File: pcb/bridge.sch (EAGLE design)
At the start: 38 parts, among them IC2 LM358D, IC3 78L05SMD, X1 PN61729-S

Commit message: bridge: Schematic beta version.
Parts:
- removed +12V: (no value), con-ptr500:AK500/2
- removed C10, C11: 22u, rcl:CPOL-EUE2,5-6E
- removed C12, C13, C9: 100n, rcl:C-EUC1210
- removed D1, D2: 3V6, diode:ZENER-DIODEDO34-7
- removed IC3: 78L05SMD, linear:78L05SMD
- removed ISP: (no value), pinhead:PINHD-2X5
- removed R11, R12: 68, rcl:R-EU_M1206
- removed R13: 1k5, rcl:R-EU_M1206
- removed R14: 10k, rcl:R-EU_M1206
- removed R15: 1k, rcl:R-EU_M1206
- removed X1: PN61729-S, con-berg:PN61729-S
- added 12V: 1751248, con-phoenix-350:1751248
- added C1, C2: 4u7, rcl:CPOL-EUB/3528-21W
- added C3, C4: 100n, rcl:C-EUC1206
- added C5: 47u, rcl:CPOL-EUC/6032-28W
- added U$1: ARDUINO_PRO_MICRO, sparkfun-boards:ARDUINO_PRO_MICRO
- RSENSE: value (none) -> 1751248; device con-ptr500:AK500/2 -> con-phoenix-350:1751248
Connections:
- removed net N$3: LCD1.VO, R14.1, R15.2
- removed net N$5: D2.C, R11.2, R13.1, X1.2
- removed net N$6: D1.C, R12.2, X1.3
- removed net PB0: LCD1.DB5
- removed net PB1: LCD1.DB6
- removed net PB2: LCD1.DB7
- removed net PB3: ISP.1
- removed net PB4: ISP.9
- removed net PB5: ISP.7
- removed net PC0: R7.2
- removed net PC1: C6.1, R1.1, R2.2
- removed net PC3: BUS.4, R10.1
- removed net PC4: BUS.3, R9.1
- removed net PC5: BUS.5, R8.1
- removed net PD0: S1.S, S1.S1
- removed net PD1: S2.S, S2.S1
- removed net PD2: S3.S, S3.S1
- removed net PD3: R11.1
- removed net PD4: R12.1
- removed net PD5: LCD1.RS
- removed net PD6: LCD1.E
- removed net PD7: LCD1.DB4
- removed net RESET: ISP.5
- new net ACURR: C2.+, C3.1, R7.2, U$1.*9
- new net AVLTG: C1.+, C6.1, R1.1, R2.2, U$1.A3
- new net BTN1: S3.S, S3.S1, U$1.*6
- new net BTN2: S2.S, S2.S1, U$1.7
- new net BTN3: S1.S, S1.S1, U$1.8
- new net DDB4: LCD1.DB4, U$1.13(SCK)
- new net DDB5: LCD1.DB5, U$1.12(MISO)
- new net DDB6: LCD1.DB6, U$1.11(MOSI)
- new net DDB7: LCD1.DB7, U$1.*10
- new net DE: LCD1.E, U$1.A0
- new net DRS: LCD1.RS, U$1.A2
- new net DRW: LCD1.R/W, U$1.A1
- new net RX: U$1.RXI
- new net SCL: BUS.5, R8.1, U$1.*3
- new net SDA: BUS.3, R9.1, U$1.2
- new net STOP: BUS.4, R10.1, U$1.4
- new net TX: U$1.TXO
- net +12V: now also 12V-1.K, U$1.RAW; no longer +12V-1.KL, C13.2, IC3G$1.VIN
- net +5V: now also C4.1, C5.+, U$1.VCC; no longer C10.+, C11.+, C12.2, C9.2, IC3G$1.VOUT, R13.2, R14.2
- net GND: now also 12V-2.K, C1.-, C2.-, C3.2, C4.2, C5.-, LCD1.VO, U$1.GND, U$1.GND@1, U$1.GND@2; no longer +12V-2.KL, C10.-, C11.-, C12.1, C13.1, C9.1, D1.A, D2.A, IC3G$1.GND@1, IC3G$1.GND@2, IC3G$1.GND@3, IC3G$1.GND@4, ISP.10, ISP.4, ISP.6, ISP.8, LCD1.R/W, R15.1, X1.4, X1.S1, X1.S2
- net N$21: now also RSENSE-2.K; no longer RSENSE-1.KL
- net N$29: now also RSENSE-1.K; no longer RSENSE-2.KL
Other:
- note added: "todo: dostosować do 2.56 V"
- moved on the sheet: C14, C6, C7, C8, IC2A, IC2B, R16, R3, R4, R5, R6, R7

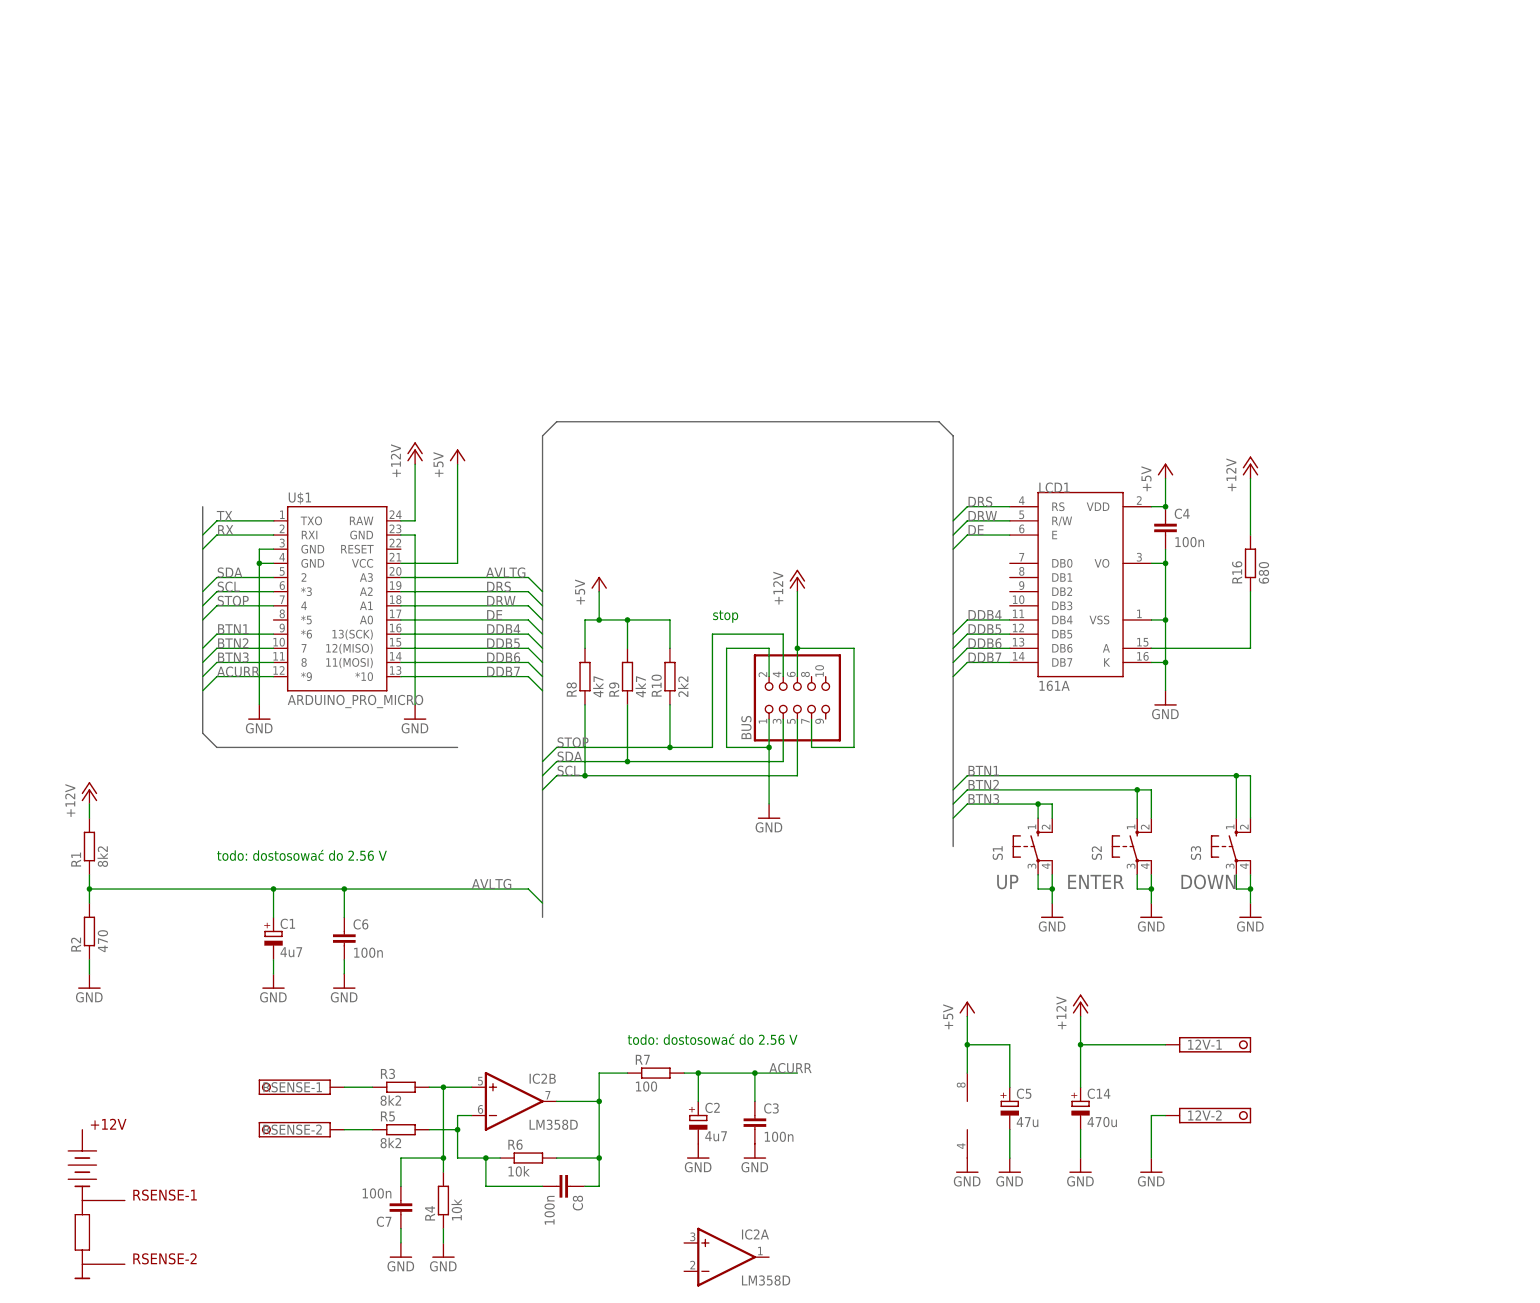
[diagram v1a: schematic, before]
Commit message: bridge: Update schematic positions and numbering.
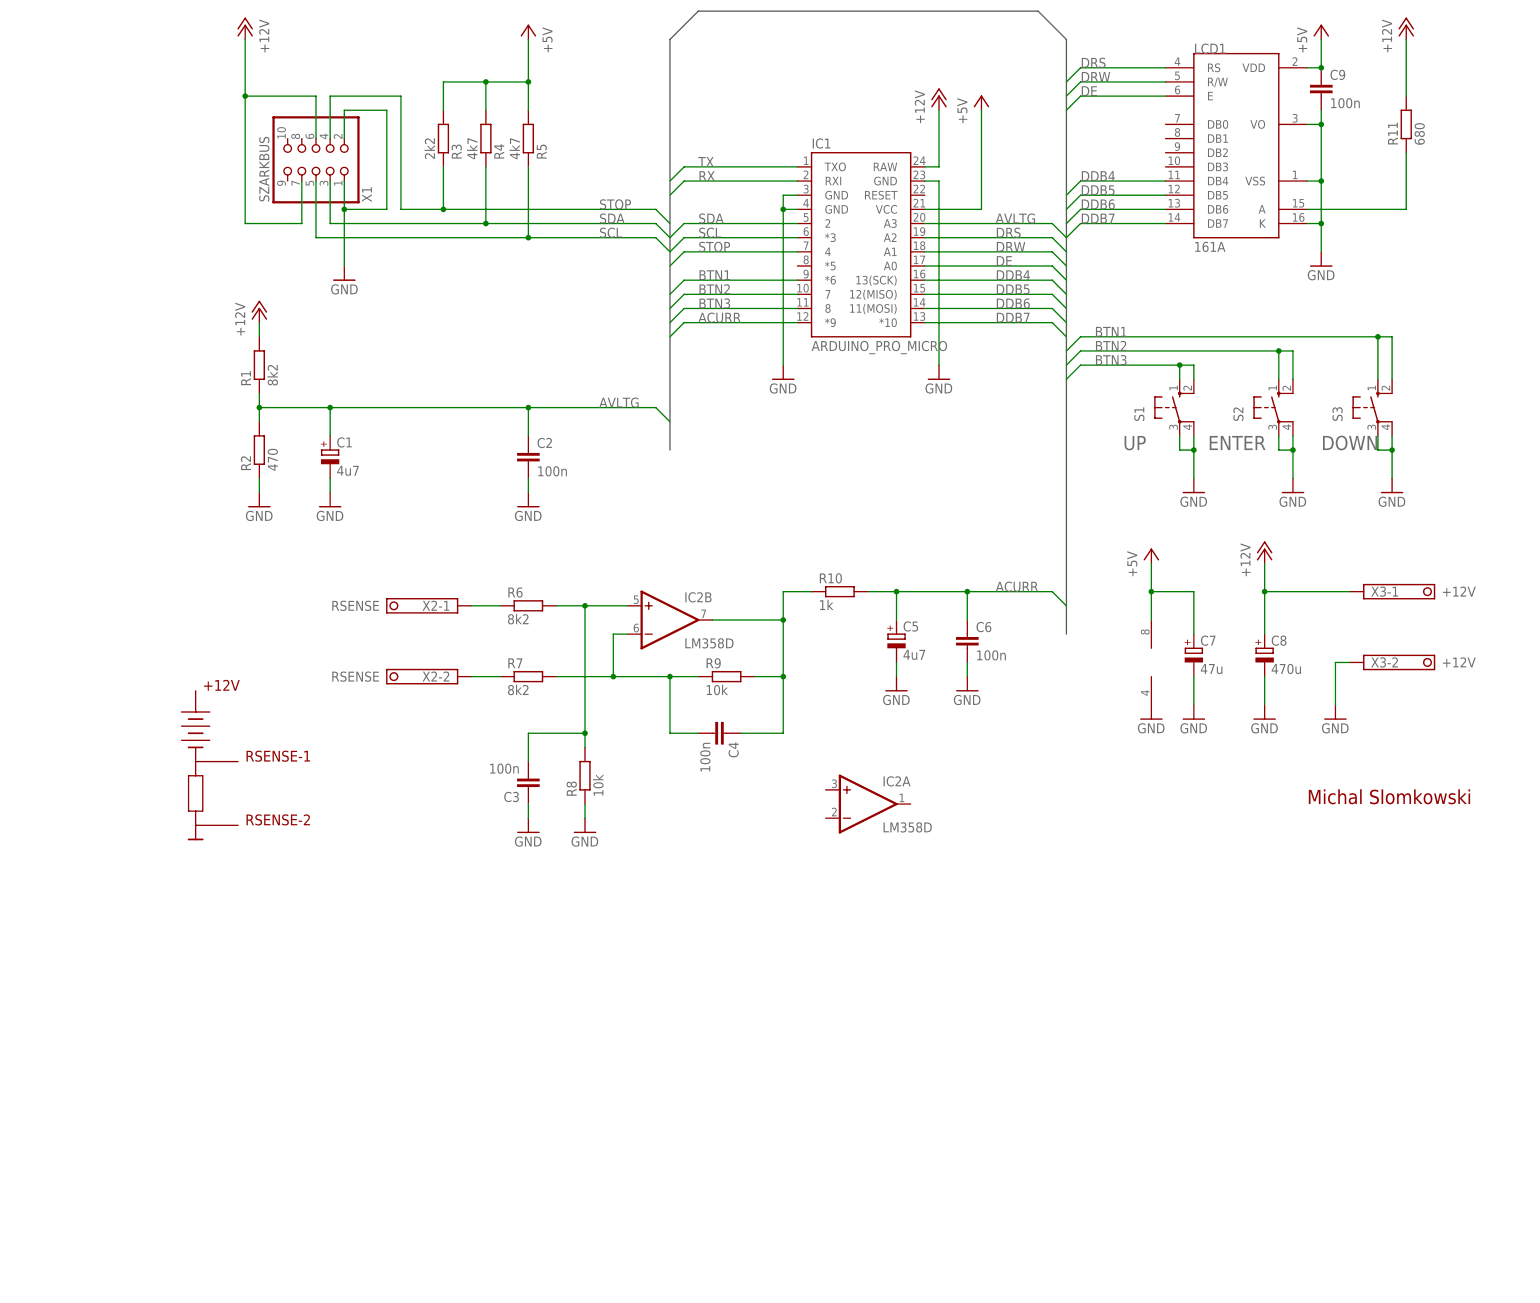
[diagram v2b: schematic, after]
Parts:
- removed 12V, RSENSE: 1751248, con-phoenix-350:1751248
- removed BUS: (no value), pinhead:PINHD-2X5
- removed C14: 470u, rcl:CPOL-EUE5-10.5
- removed R16: 680, rcl:R-EU_0207/12
- removed U$1: ARDUINO_PRO_MICRO, sparkfun-boards:ARDUINO_PRO_MICRO
- added C9: 100n, rcl:C-EUC1206
- added IC1: ARDUINO_PRO_MICRO, sparkfun-boards:ARDUINO_PRO_MICRO
- added R11: 680, rcl:R-EU_0207/12
- added X1: SZARKBUS, pinhead:PINHD-2X5
- added X2: RSENSE, con-phoenix-350:1751248
- added X3: +12V, con-phoenix-350:1751248
- C2: value 4u7 -> 100n; device rcl:CPOL-EUB/3528-21W -> rcl:C-EUC1206
- C3: device rcl:C-EUC1206 -> rcl:C-EUC1210
- C5: value 47u -> 4u7; device rcl:CPOL-EUC/6032-28W -> rcl:CPOL-EUB/3528-21W
- C7: value 100n -> 47u; device rcl:C-EUC1210 -> rcl:CPOL-EUC/6032-28W
- C8: value 100n -> 470u; device rcl:C-EUC1206 -> rcl:CPOL-EUE5-10.5
- R10: value 2k2 -> 1k
- R3: value 8k2 -> 2k2
- R4: value 10k -> 4k7
- R5: value 8k2 -> 4k7
- R6: value 10k -> 8k2
- R7: value 100 -> 8k2
- R8, R9: value 4k7 -> 10k
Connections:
- net +12V: now also C8.+, IC1.RAW, R11.2, X1.6, X1.7, X3-1.K; no longer 12V-1.K, BUS.6, BUS.7, C14.+, R16.2, U$1.RAW
- net +5V: now also C7.+, C9.1, IC1.VCC, R3.2, R4.2, R5.2; no longer C4.1, C5.+, R10.2, R8.2, R9.2, U$1.VCC
- net ACURR: now also C5.+, C6.1, IC1.*9, R10.2; no longer C2.+, C3.1, R7.2, U$1.*9
- net AVLTG: now also C2.1, IC1.A3; no longer C6.1, U$1.A3
- net BTN1: now also IC1.*6; no longer U$1.*6
- net BTN2: now also IC1.7; no longer U$1.7
- net BTN3: now also IC1.8; no longer U$1.8
- net DDB4: now also IC1.13(SCK); no longer U$1.13(SCK)
- net DDB5: now also IC1.12(MISO); no longer U$1.12(MISO)
- net DDB6: now also IC1.11(MOSI); no longer U$1.11(MOSI)
- net DDB7: now also IC1.*10; no longer U$1.*10
- net DE: now also IC1.A0; no longer U$1.A0
- net DRS: now also IC1.A2; no longer U$1.A2
- net DRW: now also IC1.A1; no longer U$1.A1
- net GND: now also C2.2, C3.1, C7.-, C8.-, C9.2, IC1.GND, IC1.GND@1, IC1.GND@2, R8.1, X1.1, X1.2, X3-2.K; no longer 12V-2.K, BUS.1, BUS.2, C14.-, C2.-, C3.2, C4.2, C7.1, R4.1, U$1.GND, U$1.GND@1, U$1.GND@2
- net N$1: now also C3.2, R6.2, R8.2; no longer C7.2, R3.2, R4.2
- net N$2: now also R11.1; no longer R16.1
- net N$21: now also R7.1, X2-2.K; no longer R5.1, RSENSE-2.K
- net N$29: now also R6.1, X2-1.K; no longer R3.1, RSENSE-1.K
- net N$4: now also C4.2, R7.2, R9.1; no longer C8.2, R5.2, R6.1
- net NET3: now also C4.1, R10.1, R9.2; no longer C8.1, R6.2, R7.1
- net RX: now also IC1.RXI; no longer U$1.RXI
- net SCL: now also IC1.*3, R5.1, X1.5; no longer BUS.5, R8.1, U$1.*3
- net SDA: now also IC1.2, R4.1, X1.3; no longer BUS.3, R9.1, U$1.2
- net STOP: now also IC1.4, R3.1, X1.4; no longer BUS.4, R10.1, U$1.4
- net TX: now also IC1.TXO; no longer U$1.TXO
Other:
- note added: "Michal Slomkowski"
- note removed: "stop"
- note removed: "todo: dostosować do 2.56 V"
- moved on the sheet: C1, C3, C4, C5, C6, IC2A, IC2B, LCD1, R1, R10, R2, R3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

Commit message: bridge: Mock PCB ready.
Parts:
- added C10: 100n, rcl:C-EUC1206
- C8: device rcl:CPOL-EUE5-10.5 -> rcl:CPOL-EUE5-8.5
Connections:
- net +5V: now also C10.1
- net ACURR: now also IC1.A2; no longer IC1.*9
- net DDB4: now also IC1.12(MISO); no longer IC1.13(SCK)
- net DDB5: now also IC1.11(MOSI); no longer IC1.12(MISO)
- net DDB6: now also IC1.*10; no longer IC1.11(MOSI)
- net DDB7: now also IC1.*9; no longer IC1.*10
- net DE: now also IC1.13(SCK); no longer IC1.A0
- net DRS: now also IC1.A1; no longer IC1.A2
- net DRW: now also IC1.A0; no longer IC1.A1
- net GND: now also C10.2
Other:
- moved on the sheet: C7, C8, X3-1, X3-2

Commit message: bridge: Board ready beta.
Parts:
- added C11: 100n, rcl:C-EUC1206
- C10: value 100n -> 470u; device rcl:C-EUC1206 -> rcl:CPOL-EUE5-8.5
- C7: value 47u -> 100n; device rcl:CPOL-EUC/6032-28W -> rcl:C-EUC1206
- C8: value 470u -> 47u; device rcl:CPOL-EUE5-8.5 -> rcl:CPOL-EUC/6032-28W
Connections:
- net +12V: now also C10.+; no longer C8.+
- net +5V: now also C11.1, C7.1, C8.+; no longer C10.1, C7.+
- net GND: now also C10.-, C11.2, C7.2; no longer C10.2, C7.-
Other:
- moved on the sheet: C8, C9
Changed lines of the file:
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@@
 <part name="GND13" library="supply1" deviceset="GND" device=""/>
 <part name="P+7" library="supply1" deviceset="+12V" device=""/>
-<part name="C8" library="rcl" deviceset="CPOL-EU" device="E5-8.5" value="470u"/>
+<part name="C10" library="rcl" deviceset="CPOL-EU" device="E5-8.5" value="470u"/>
 <part name="GND20" library="supply1" deviceset="GND" device=""/>
 <part name="P+11" library="supply1" deviceset="+12V" device=""/>
@@
 <part name="X2" library="con-phoenix-350" deviceset="1751248" device="" value="RSENSE"/>
 <part name="X3" library="con-phoenix-350" deviceset="1751248" device="" value="+12V"/>
-<part name="C9" library="rcl" deviceset="C-EU" device="C1206" value="100n"/>
-<part name="C7" library="rcl" deviceset="CPOL-EU" device="C/6032-28W" value="47u"/>
+<part name="C11" library="rcl" deviceset="C-EU" device="C1206" value="100n"/>
+<part name="C8" library="rcl" deviceset="CPOL-EU" device="C/6032-28W" value="47u"/>
 <part name="GND9" library="supply1" deviceset="GND" device=""/>
 <part name="GND10" library="supply1" deviceset="GND" device=""/>
 <part name="P+5" library="supply1" deviceset="+5V" device=""/>
-<part name="C10" library="rcl" deviceset="C-EU" device="C1206" value="100n"/>
+<part name="C9" library="rcl" deviceset="C-EU" device="C1206" value="100n"/>
 <part name="GND14" library="supply1" deviceset="GND" device=""/>
+<part name="C7" library="rcl" deviceset="C-EU" device="C1206" value="100n"/>
+<part name="GND15" library="supply1" deviceset="GND" device=""/>
 </parts>
 <sheets>
@@
 <instance part="GND13" gate="1" x="233.68" y="76.2"/>
 <instance part="P+7" gate="1" x="236.22" y="160.02"/>
-<instance part="C8" gate="G$1" x="215.9" y="48.26"/>
+<instance part="C10" gate="G$1" x="215.9" y="48.26"/>
 <instance part="GND20" gate="1" x="215.9" y="35.56"/>
 <instance part="P+11" gate="1" x="215.9" y="66.04"/>
@@
 <instance part="IC1" gate="G$1" x="137.16" y="119.38"/>
 <instance part="FRAME1" gate="G$1" x="0" y="0"/>
-<instance part="GND2" gate="1" x="124.46" y="96.52"/>
-<instance part="GND3" gate="1" x="152.4" y="96.52"/>
+<instance part="GND2" gate="1" x="124.46" y="88.9"/>
+<instance part="GND3" gate="1" x="152.4" y="88.9"/>
 <instance part="P+1" gate="1" x="152.4" y="147.32"/>
 <instance part="P+4" gate="1" x="160.02" y="147.32"/>
@@
 <instance part="X3" gate="-1" x="231.14" y="58.42"/>
 <instance part="X3" gate="-2" x="231.14" y="45.72"/>
-<instance part="C9" gate="G$1" x="220.98" y="149.86"/>
+<instance part="C11" gate="G$1" x="220.98" y="149.86"/>
 <instance part="IC2" gate="P" x="187.96" y="45.72"/>
-<instance part="C7" gate="G$1" x="195.58" y="48.26"/>
+<instance part="C8" gate="G$1" x="195.58" y="48.26"/>
 <instance part="GND9" gate="1" x="187.96" y="35.56"/>
 <instance part="GND10" gate="1" x="195.58" y="35.56"/>
 <instance part="P+5" gate="1" x="187.96" y="66.04"/>
-<instance part="C10" gate="G$1" x="203.2" y="48.26"/>
+<instance part="C9" gate="G$1" x="203.2" y="48.26"/>
 <instance part="GND14" gate="1" x="203.2" y="35.56"/>
+<instance part="C7" gate="G$1" x="160.02" y="99.06"/>
+<instance part="GND15" gate="1" x="160.02" y="88.9"/>
 </instances>
 <busses>
@@
 <wire x1="220.98" y1="142.24" x2="220.98" y2="132.08" width="0.1524" layer="91"/>
 <junction x="220.98" y="132.08"/>
-<pinref part="C9" gate="G$1" pin="2"/>
+<pinref part="C11" gate="G$1" pin="2"/>
 <wire x1="220.98" y1="144.78" x2="220.98" y2="142.24" width="0.1524" layer="91"/>
 <junction x="220.98" y="142.24"/>
@@
 <wire x1="215.9" y1="38.1" x2="215.9" y2="43.18" width="0.1524" layer="91"/>
 <pinref part="GND20" gate="1" pin="GND"/>
-<pinref part="C8" gate="G$1" pin="-"/>
+<pinref part="C10" gate="G$1" pin="-"/>
 </segment>
 <segment>
@@
 <wire x1="124.46" y1="129.54" x2="124.46" y2="127" width="0.1524" layer="91"/>
 <pinref part="IC1" gate="G$1" pin="GND"/>
-<wire x1="124.46" y1="127" x2="124.46" y2="99.06" width="0.1524" layer="91"/>
+<wire x1="124.46" y1="127" x2="124.46" y2="91.44" width="0.1524" layer="91"/>
 <wire x1="127" y1="127" x2="124.46" y2="127" width="0.1524" layer="91"/>
 <junction x="124.46" y="127"/>
@@
 <segment>
 <pinref part="GND3" gate="1" pin="GND"/>
-<wire x1="152.4" y1="99.06" x2="152.4" y2="132.08" width="0.1524" layer="91"/>
+<wire x1="152.4" y1="91.44" x2="152.4" y2="132.08" width="0.1524" layer="91"/>
 <pinref part="IC1" gate="G$1" pin="GND@2"/>
 <wire x1="152.4" y1="132.08" x2="149.86" y2="132.08" width="0.1524" layer="91"/>
@@
 </segment>
 <segment>
-<pinref part="C7" gate="G$1" pin="-"/>
+<pinref part="C8" gate="G$1" pin="-"/>
 <pinref part="GND10" gate="1" pin="GND"/>
 <wire x1="195.58" y1="38.1" x2="195.58" y2="43.18" width="0.1524" layer="91"/>
 </segment>
 <segment>
-<pinref part="C10" gate="G$1" pin="2"/>
+<pinref part="C9" gate="G$1" pin="2"/>
 <pinref part="GND14" gate="1" pin="GND"/>
 <wire x1="203.2" y1="43.18" x2="203.2" y2="38.1" width="0.1524" layer="91"/>
+</segment>
+<segment>
+<pinref part="C7" gate="G$1" pin="2"/>
+<pinref part="GND15" gate="1" pin="GND"/>
+<wire x1="160.02" y1="91.44" x2="160.02" y2="93.98" width="0.1524" layer="91"/>
 </segment>
 </net>
@@
 <pinref part="P+6" gate="1" pin="+5V"/>
 <pinref part="LCD1" gate="G$1" pin="VDD"/>
-<pinref part="C9" gate="G$1" pin="1"/>
+<pinref part="C11" gate="G$1" pin="1"/>
 <junction x="220.98" y="152.4"/>
 </segment>
@@
 <wire x1="149.86" y1="127" x2="160.02" y2="127" width="0.1524" layer="91"/>
 <wire x1="160.02" y1="127" x2="160.02" y2="144.78" width="0.1524" layer="91"/>
-</segment>
-<segment>
-<pinref part="C7" gate="G$1" pin="+"/>
+<pinref part="C7" gate="G$1" pin="1"/>
+<wire x1="160.02" y1="127" x2="160.02" y2="101.6" width="0.1524" layer="91"/>
+<junction x="160.02" y="127"/>
+</segment>
+<segment>
+<pinref part="C8" gate="G$1" pin="+"/>
 <wire x1="195.58" y1="50.8" x2="195.58" y2="58.42" width="0.1524" layer="91"/>
 <wire x1="195.58" y1="58.42" x2="187.96" y2="58.42" width="0.1524" layer="91"/>
@@
 <wire x1="187.96" y1="63.5" x2="187.96" y2="58.42" width="0.1524" layer="91"/>
 <junction x="187.96" y="58.42"/>
-<pinref part="C10" gate="G$1" pin="1"/>
+<pinref part="C9" gate="G$1" pin="1"/>
 <wire x1="203.2" y1="50.8" x2="203.2" y2="58.42" width="0.1524" layer="91"/>
 <wire x1="203.2" y1="58.42" x2="195.58" y2="58.42" width="0.1524" layer="91"/>
@@
 <wire x1="228.6" y1="58.42" x2="215.9" y2="58.42" width="0.1524" layer="91"/>
 <junction x="215.9" y="58.42"/>
-<pinref part="C8" gate="G$1" pin="+"/>
+<pinref part="C10" gate="G$1" pin="+"/>
 <pinref part="P+11" gate="1" pin="+12V"/>
 <pinref part="X3" gate="-1" pin="K"/>
